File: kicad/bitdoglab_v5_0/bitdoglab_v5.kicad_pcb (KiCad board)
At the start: 2 copper layers, 87.9 x 123.9 mm, 75 parts, among them J1 Conn_01x20_Socket, J10 3V3, J100 JST_EH_B4B-EH-A_1x04_P2.50mm_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, J101 JST_EH_B4B-EH-A_1x04_P2.50mm_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, J11 5V-VSYS, J12 Conn_01x05_Pin, J13 Conn_01x05_Pin, J14 5x5 Matrix led, J15 0, J16 1, J17 2, J18 3, J19 JOYSTICK, J2 conector_idc, J3 Conn_01x20_Socket, J4 jumper_mic, J5 Conn_01x05_Pin, J6 Conn_01x05_Pin, J7 GND, J8 ANA-IN, J9 GND, Q1 DMG2305UX-13, Q2 BC337, Q3 BC337, SW1 Reset, SW2 Botão, SW3 Button_B, U1 3.3v_tht, U4 MIC

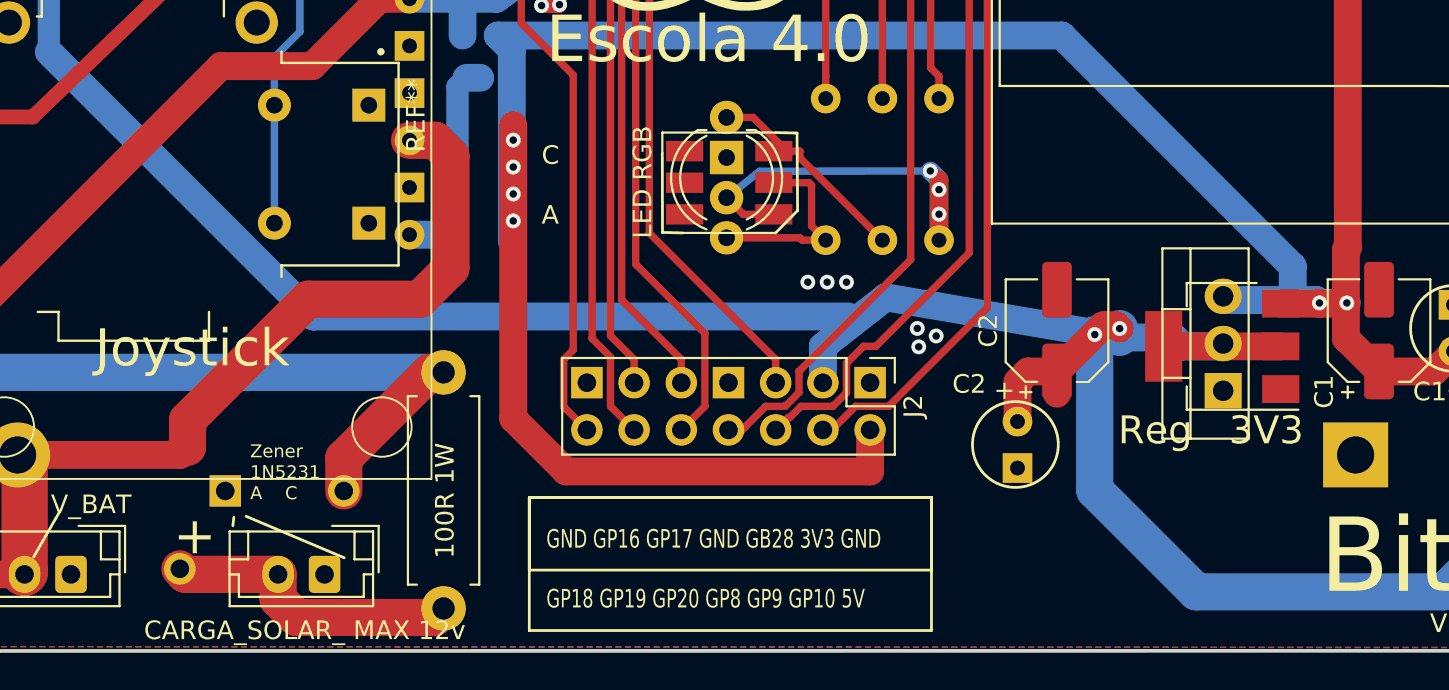
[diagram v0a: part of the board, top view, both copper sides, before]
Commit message: Sincronizar layout com esquematico - parte 1
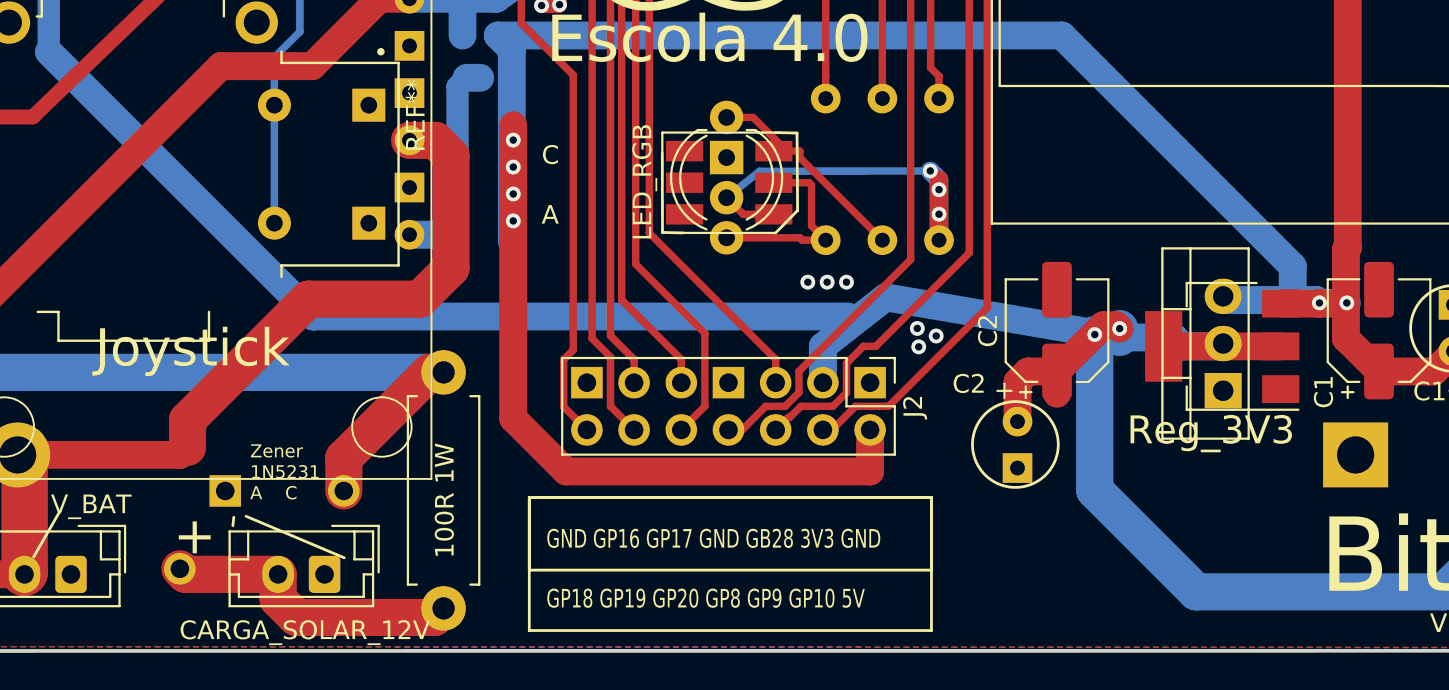
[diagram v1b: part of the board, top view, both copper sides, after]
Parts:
- CARGA_SOLAR_12V: renamed from CARGA_SOLAR_ MAX 12v; value JST_EH_B2B-EH-A_1x02_P2.50mm_Vertical -> solar
- Charge_DisCharge1: renamed from Charge DisCharge
- LED_RGB: renamed from LED RGB
- R_1W: renamed from REF**; value R_Axial_DIN0411_L9.9mm_D3.6mm_P12.70mm_Horizontal -> 100
- Rb_150: renamed from Rb 150
- Reg_3V3: renamed from Reg   3V3
- Rg_220: renamed from Rg 220; value 150 -> 220
- Rr_220: renamed from Rr 220
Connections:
- net /VSYS_EXT renamed VSYS_EXT
- D2 pad 1: Net-(D1-RA) -> Net-(D2-RA)
- D2 pad 3: Net-(D1-BA) -> Net-(D2-BA)
- D2 pad 4: Net-(D1-GA) -> Net-(D2-GA)
- J13 pad 5: /AGND_EXT -> GNDREF
- J15 pad 1: /GP0_EXT -> /GP03_EXT
- J15 pad 2: /GP0_EXT -> /GP03_EXT
- J16 pad 1: /GP01_EXT -> /GP02_EXT
- J16 pad 2: /GP01_EXT -> /GP02_EXT
- J17 pad 1: /GP02_EXT -> /GP01_EXT
- J17 pad 2: /GP02_EXT -> /GP01_EXT
- J18 pad 1: /GP03_EXT -> /GP0_EXT
- J18 pad 2: /GP03_EXT -> /GP0_EXT
- J6 pad 1: /AGND_EXT -> GNDREF
- J7 pad 1: /AGND_EXT -> GNDREF
- J7 pad 2: /AGND_EXT -> GNDREF
- Q1 pad 3: Net-(Q1-D) -> Net-(Charge DisCharge1-OUT5V)
- Rb_150 pad 1: Net-(D1-BA) -> Net-(D2-BA)
- Reg_3V3 pad 4: +3.3V -> (no net)
- Rg_220 pad 1: Net-(D1-GA) -> Net-(D2-GA)
- Rr_220 pad 1: Net-(D1-RA) -> Net-(D2-RA)

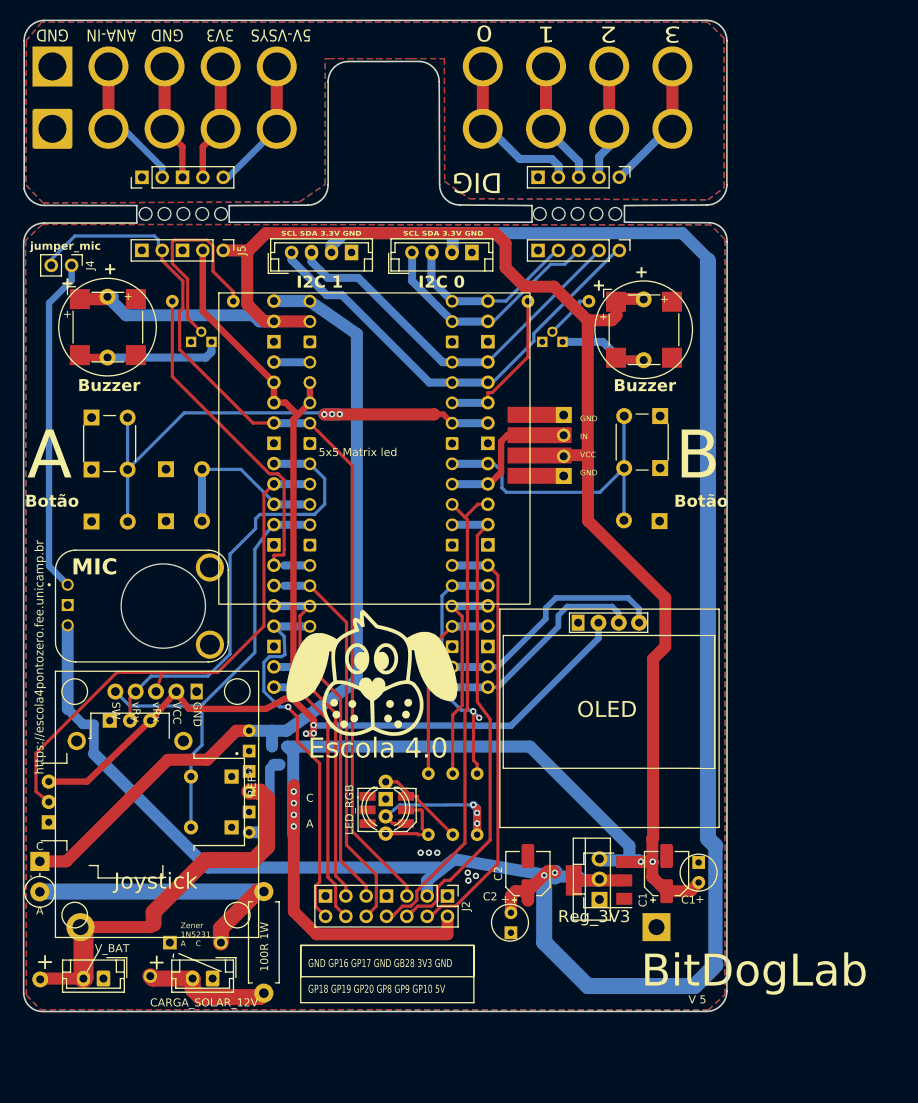
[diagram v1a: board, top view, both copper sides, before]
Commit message: Sincronizar layout com esquematico - parte 2
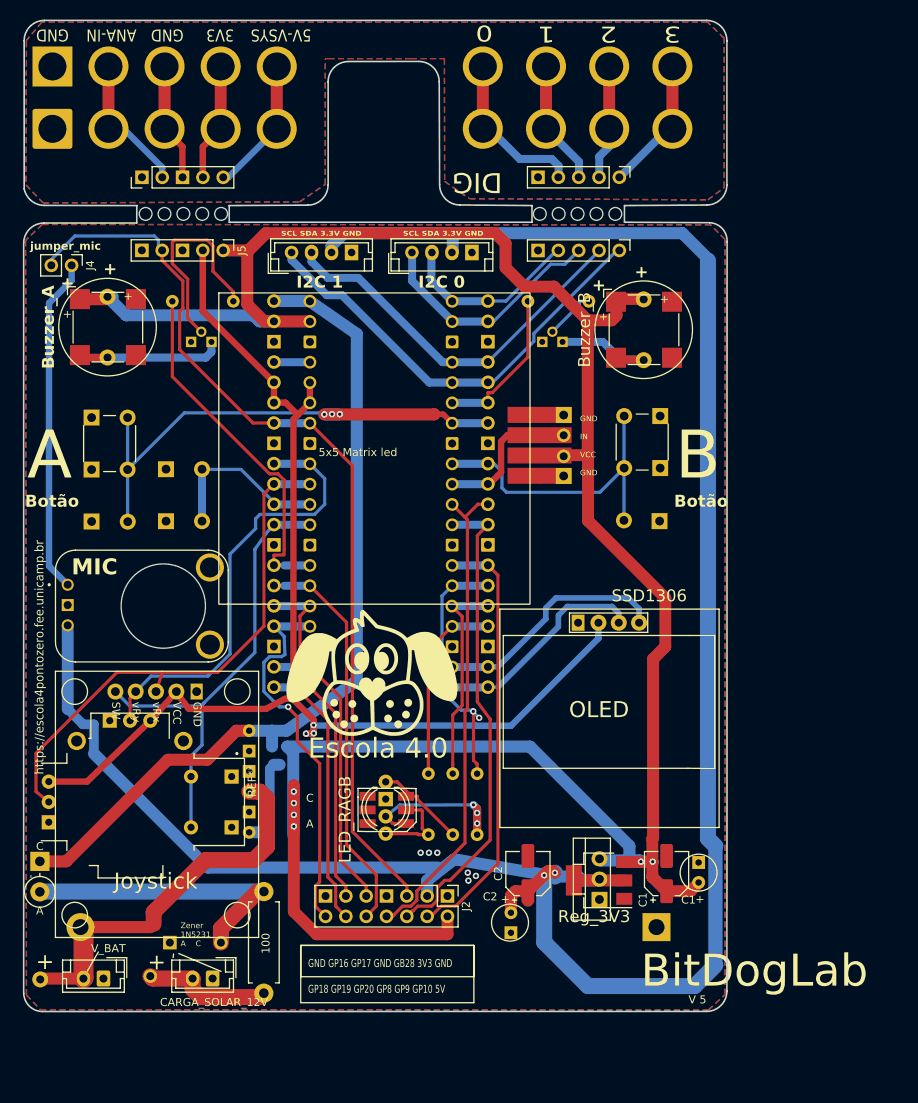
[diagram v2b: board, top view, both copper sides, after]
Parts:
- CARGA_SOLAR1: renamed from CARGA_SOLAR_12V; value solar -> CARGA_SOLAR_12V
- D1: renamed from LED_RGB; value LED_RGB_SMD -> LED_RGB
- V_BAT1: renamed from V_BAT; value JST_EH_B2B-EH-A_1x02_P2.50mm_Vertical -> V_BAT
- renumbered Buzzer to BZ2, OLED to OLED1, R_1W to R_1W1
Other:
- board text removed: "100R 1W"
- board text removed: "Buzzer"
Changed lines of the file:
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@@
         (effects (font (size 1 1) (thickness 0.15)))
     )
-    (fp_text value "Buzzer_B" (at 3.8 7.4 90) (layer "F.Fab") hide
-        (effects (font (size 1 1) (thickness 0.15)))
+    (fp_text value "Buzzer_B" (at 3.8 7.4 90) (layer "F.SilkS")
+        (effects (font (size 1.5 1.5) (thickness 0.3)))
     )
     (fp_text user "+" (at -0.01 -2.54 90) (layer "F.SilkS")
@@
     (tags "connector JST EH vertical")
     (attr through_hole)
-    (fp_text reference "CARGA_SOLAR_12V" (at 1.065825 -3.018428) (layer "F.SilkS")
+    (fp_text reference "CARGA_SOLAR1" (at 1.065825 -3.018428) (layer "F.Fab") hide
         (effects (font (size 1 1) (thickness 0.15)))
     )
-    (fp_text value "solar" (at 1.25 3.4) (layer "F.Fab") hide
+    (fp_text value "CARGA_SOLAR_12V" (at -0.1718 -2.97) (layer "F.SilkS")
         (effects (font (size 1 1) (thickness 0.15)))
     )
@@
     (property "ki_keywords" "quartz resonator ceramic")
     (attr smd)
-    (fp_text reference "BZ4" (at -0.1524 7.122) (layer "F.SilkS") hide
+    (fp_text reference "BZ4" (at -0.1524 7.122) (layer "F.Fab") hide
         (effects (font (size 1 1) (thickness 0.15)))
     )
-    (fp_text value "Buzzer_B_SMD" (at 0.1 6) (layer "F.Fab") hide
+    (fp_text value "Buzzer_B_SMD" (at 0.1 6) (layer "F.SilkS") hide
         (effects (font (size 1.5 1.5) (thickness 0.3) bold))
     )
@@
     (property "ki_keywords" "quartz resonator ceramic")
     (attr smd)
-    (fp_text reference "Buzzer" (at 0.1524 7.295) (layer "F.SilkS")
+    (fp_text reference "BZ2" (at 0.1524 7.295) (layer "F.Fab")
         (effects (font (size 1.5 1.5) (thickness 0.3) bold))
     )
-    (fp_text value "Buzzer_A_SMD" (at 0.1 6) (layer "F.Fab")
-        (effects (font (size 1 1) (thickness 0.15)))
+    (fp_text value "Buzzer_A_SMD" (at 0.4375 7.0545) (layer "F.SilkS") hide
+        (effects (font (size 1.5 1.5) (thickness 0.3)))
     )
     (fp_text user "+" (at -5.1 -1.6 270) (layer "F.SilkS")
@@
     (property "ki_keywords" "LED RGB diode")
     (attr through_hole)
-    (fp_text reference "D2" (at 3.2385 -3.96 90) (layer "F.SilkS") hide
+    (fp_text reference "D2" (at 3.2385 -3.96 90) (layer "F.Fab") hide
         (effects (font (size 1 1) (thickness 0.15)))
     )
-    (fp_text value "LED_RAGB" (at 4.699 5.08 90) (layer "F.Fab")
+    (fp_text value "LED_RAGB" (at 4.699 5.08 90) (layer "F.SilkS")
         (effects (font (size 1.5 1.5) (thickness 0.3)))
     )
@@
     (tags "Resistor Axial_DIN0411 series Axial Horizontal pin pitch 12.7mm 1W length 9.9mm diameter 3.6mm")
     (attr through_hole)
-    (fp_text reference "R_1W" (at 6.35 -2.92 90) (layer "F.SilkS") hide
+    (fp_text reference "R_1W1" (at 6.35 -2.92 90) (layer "F.Fab") hide
         (effects (font (size 1 1) (thickness 0.15)))
     )
-    (fp_text value "100" (at 6.35 2.92 90) (layer "F.Fab") hide
+    (fp_text value "100" (at 6.226 0.244 90) (layer "F.SilkS")
         (effects (font (size 1 1) (thickness 0.15)))
     )
@@
     (tags "connector JST EH vertical")
     (attr through_hole)
-    (fp_text reference "V_BAT" (at -1.0868 3.7592) (layer "F.SilkS")
+    (fp_text reference "V_BAT1" (at -1.0868 3.7592) (layer "F.Fab") hide
         (effects (font (size 1 1) (thickness 0.15)))
     )
-    (fp_text value "JST_EH_B2B-EH-A_1x02_P2.50mm_Vertical" (at 1.25 3.4) (layer "F.Fab") hide
+    (fp_text value "V_BAT" (at -0.609 3.761) (layer "F.SilkS")
         (effects (font (size 1 1) (thickness 0.15)))
     )
@@
     (property "ki_keywords" "quartz resonator ceramic")
     (attr through_hole)
-    (fp_text reference "BZ1" (at 3.8 -7.2 90) (layer "F.SilkS") hide
+    (fp_text reference "BZ1" (at 3.8 -7.2 90) (layer "F.Fab") hide
         (effects (font (size 1 1) (thickness 0.15)))
     )
-    (fp_text value "Buzzer_A" (at 3.8 7.4 90) (layer "F.Fab")
+    (fp_text value "Buzzer_A" (at 3.8 7.4 90) (layer "F.SilkS")
         (effects (font (size 1.5 1.5) (thickness 0.3) bold))
     )
@@
     (property "partnumber" "")
     (attr through_hole)
-    (fp_text reference "OLED" (at 0 0.254) (layer "F.SilkS")
+    (fp_text reference "OLED1" (at 0 0.254) (layer "F.Fab") hide
         (effects (font (size 2 2) (thickness 0.15)))
     )
-    (fp_text value "SSD1306" (at 5.27 -13.97) (layer "F.Fab")
+    (fp_text value "SSD1306" (at 5.27 -13.97) (layer "F.SilkS")
         (effects (font (size 1.5 1.5) (thickness 0.3)))
     )
+    (fp_text user "OLED" (at -1.0038 0.2712 unlocked) (layer "F.SilkS")
+        (effects (font (size 2 2) (thickness 0.15)))
+    )
     (fp_line (start -13.4 -12.3) (end 14 -12.3)
       (stroke (width 0.12) (type solid)) (layer "F.SilkS"))
@@
     (property "partnumber" "")
     (attr smd)
-    (fp_text reference "LED_RGB" (at -4.6612 -0.0342 90) (layer "F.SilkS")
+    (fp_text reference "D1" (at -4.6612 -0.0342 90) (layer "F.Fab") hide
         (effects (font (size 1 1) (thickness 0.15)))
     )
-    (fp_text value "LED_RGB_SMD" (at 0 3.3) (layer "F.Fab")
+    (fp_text value "LED_RGB" (at 0 3.3) (layer "F.SilkS") hide
         (effects (font (size 1 1) (thickness 0.15)))
     )
@@
     (property "Sheetname" "")
     (attr through_hole)
-    (fp_text reference "Charge_DisCharge1" (at 6.9923 1.6137) (layer "B.SilkS")
+    (fp_text reference "Charge_DisCharge1" (at 6.9923 1.6137) (layer "B.Fab") hide
         (effects (font (size 1 1) (thickness 0.15)) (justify mirror))
     )
-    (fp_text value "BAT (DIS)CHARGE" (at 3.175 14.1605) (layer "B.Fab")
-        (effects (font (size 0.7 0.7) (thickness 0.05)) (justify mirror))
+    (fp_text value "BAT (DIS)CHARGE" (at 7.5511 1.4867) (layer "B.SilkS")
+        (effects (font (size 1 1) (thickness 0.15)) (justify mirror))
     )
     (fp_line (start -0.1905 -0.254) (end -0.1905 15.6845)
@@
     )
   )
-  (gr_text "100R 1W" (at 118.78 151.12 90) (layer "F.SilkS")
-    (effects (font (size 1 1) (thickness 0.15)) (justify left bottom))
-  )
   (gr_text "C\n\nA" (at 123.39 133.22) (layer "F.SilkS")
     (effects (font (size 1 1) (thickness 0.15)) (justify left bottom))
@@
     (effects (font (size 1 1) (thickness 0.15)))
   )
-  (gr_text "Buzzer" (at 165.735 77.851) (layer "F.SilkS")
-    (effects (font (size 1.5 1.5) (thickness 0.3) bold))
-  )
   (gr_text "C1" (at 171.196 142.1384) (layer "F.SilkS")

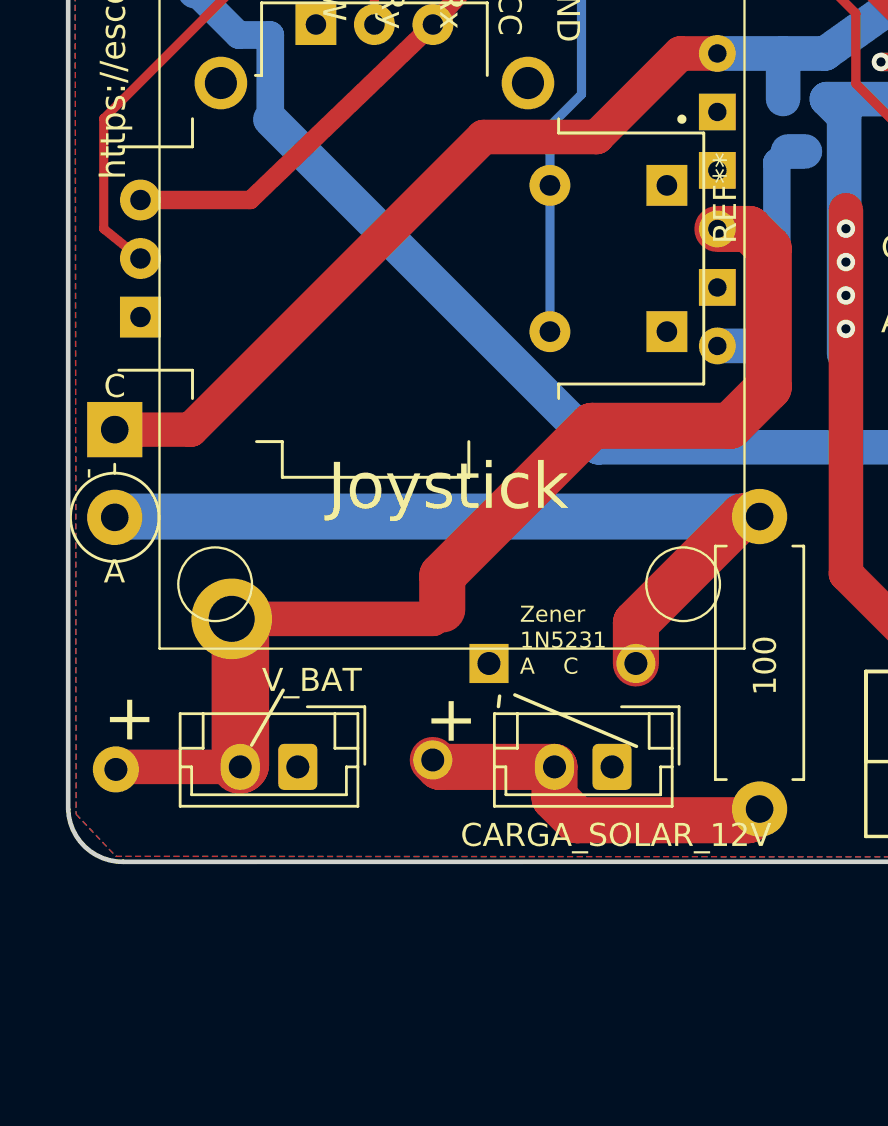
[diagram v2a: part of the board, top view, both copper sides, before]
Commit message: Sincronizar layout com esquematico - parte 3
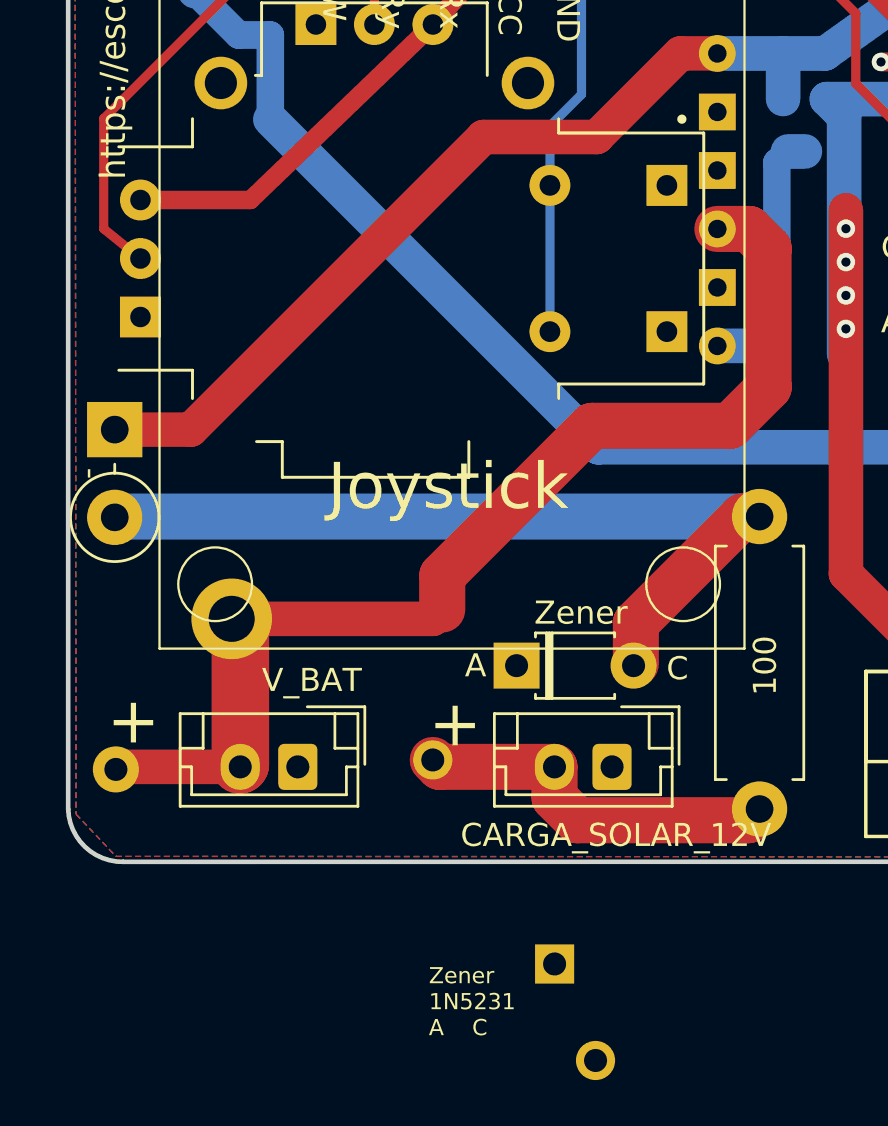
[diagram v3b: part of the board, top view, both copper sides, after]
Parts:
- added D3: Zener, Diode_THT:D_T-1_P5.08mm_Horizontal, F.Cu at (107.6, 147.6)
- D4: renamed from Diode Shottky; value D_DO-15_P3.81mm_Vertical_KathodeUp -> D Shot
- moved ? 17.3 mm to (111.0, 164.7)
- moved ? 13.4 mm to (109.2, 160.5)
- renumbered J100 to J20, J101 to J21
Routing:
- net (no net): track 37.1 -> 48.7 mm
- net Net-(Q1-D): track 11.6 -> 0.00 mm
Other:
- board text removed: "D Shot 1N5819"
